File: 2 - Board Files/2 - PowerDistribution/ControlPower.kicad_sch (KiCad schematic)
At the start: 0 parts

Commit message: Part values for power input stage
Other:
- note added: "Switching Regulator A, 16V->3.3V Switching Regulator B, 5V->3.3V IF USB 5V PRESENT: DISABLE SWITCHER A, ENABLE SWITCHER B OTHERWISE, ENABLE SWITCHER A, DISABLE SWITCHER B Ensure hold up adequate to regulate during the switch!!"
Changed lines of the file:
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@@
 (kicad_sch (version 20211123) (generator eeschema)
   (paper "A4")
+  (text "Switching Regulator A, 16V->3.3V\nSwitching Regulator B, 5V->3.3V\n\nIF USB 5V PRESENT:\n\nDISABLE SWITCHER A, ENABLE SWITCHER B\n\nOTHERWISE,\n\nENABLE SWITCHER A, DISABLE SWITCHER B\n\nEnsure hold up adequate to regulate during the switch!!"
+    (at 17.78 39.37 0)
+    (effects (font (size 1.27 1.27)) (justify left bottom))
+  )
 )

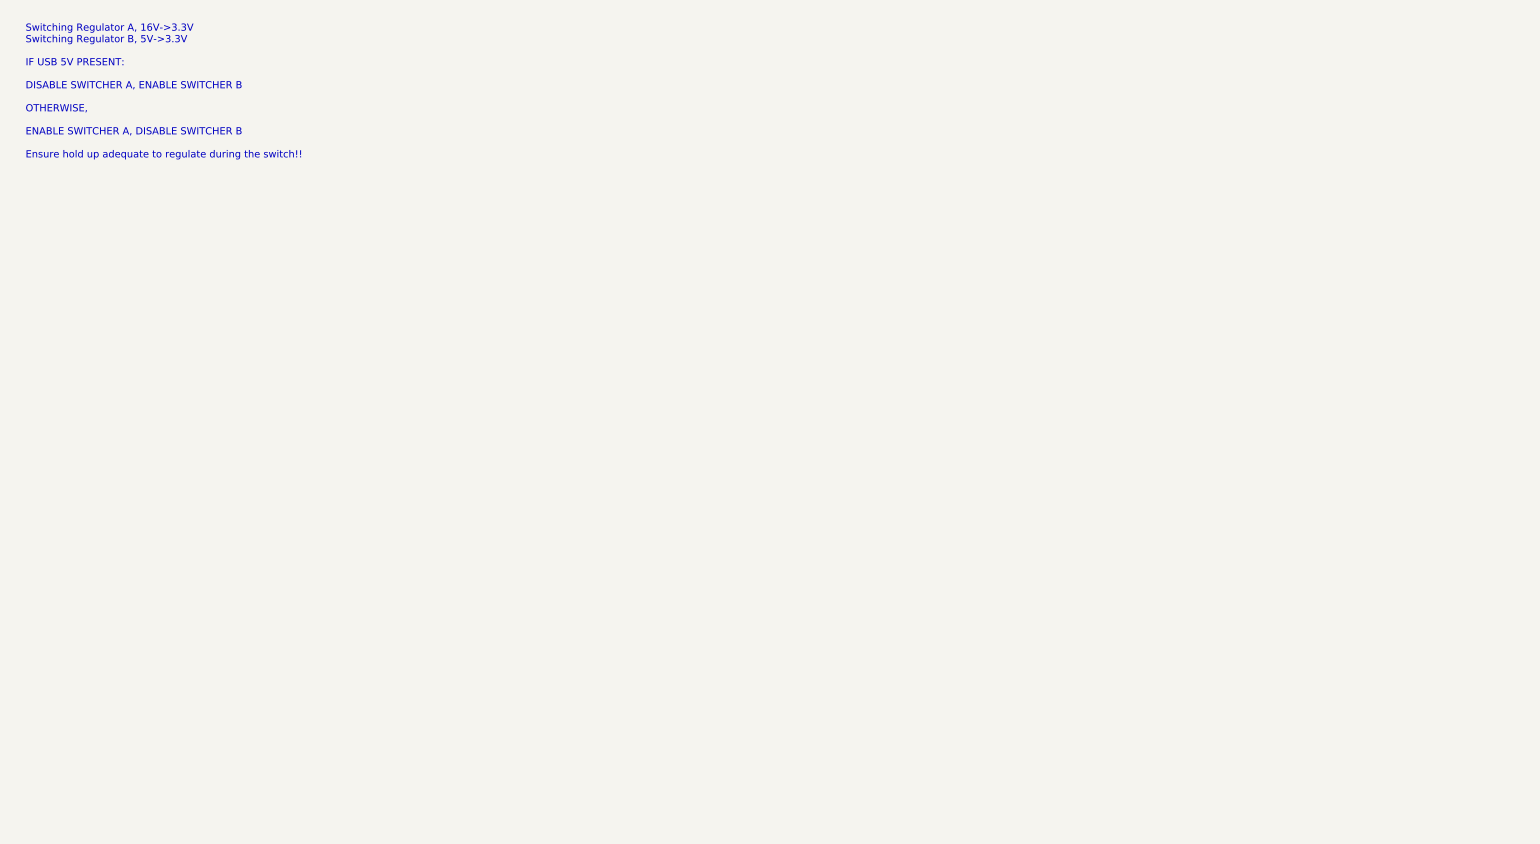
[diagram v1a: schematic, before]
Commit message: Added switching regulator
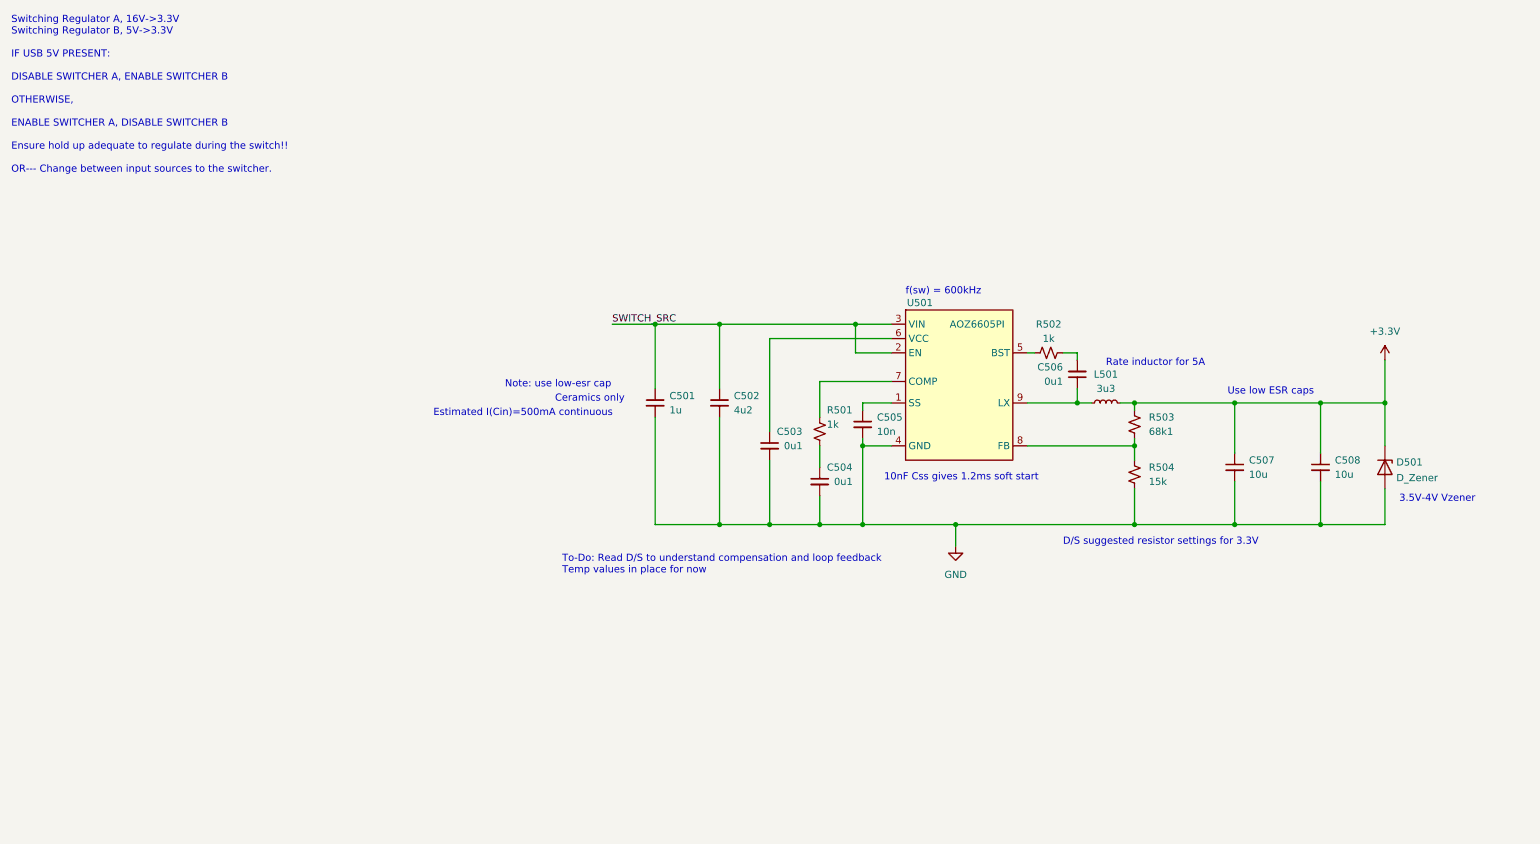
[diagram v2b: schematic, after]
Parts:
- added C501: 1u, Capacitor_SMD:C_0805_2012Metric, symbol Device:C_Small
- added C502: 4u2, Capacitor_SMD:C_0805_2012Metric, symbol Device:C_Small
- added C503, C504, C506: 0u1, Capacitor_SMD:C_0402_1005Metric, symbol Device:C_Small
- added C505: 10n, Capacitor_SMD:C_0402_1005Metric, symbol Device:C_Small
- added C507, C508: 10u, Capacitor_SMD:CP_Elec_6.3x5.4, symbol Device:C_Small
- added D501: D_Zener, Diode_SMD:D_SOD-323, symbol Device:D_Zener
- added L501: 3u3, Inductor_SMD:L_12x12mm_H4.5mm, symbol Device:L_Small
- added R501, R502: 1k, Resistor_SMD:R_0402_1005Metric, symbol Device:R_Small_US
- added R503: 68k1, Resistor_SMD:R_0402_1005Metric, symbol Device:R_Small_US
- added R504: 15k, Resistor_SMD:R_0402_1005Metric, symbol Device:R_Small_US
- added U501: AOZ6605PI, Package_SO:SOIC-8-1EP_3.9x4.9mm_P1.27mm_EP2.95x4.9mm_Mask2.71x3.4mm, symbol QuadrotorLib:AOZ6605PI
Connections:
- new net: R501.1, U501.7 (COMP)
- new net: C504.1, R501.2
- new net: C506.1, L501.1, U501.9 (LX)
- new net: C506.2, R502.1
- new net: R502.2, U501.5 (BST)
- new net: C503.1, U501.6 (VCC)
- new net: C505.1, U501.1 (SS)
- new net: R503.2, R504.1, U501.8 (FB)
- new net +3.3V: C507.1, C508.1, D501.1 (K), L501.2, R503.1
- new net GND: C501.2, C502.2, C503.2, C504.2, C505.2, C507.2, C508.2, D501.2 (A), R504.2, U501.4 (GND)
- new net SWITCH_SRC: C501.1, C502.1, U501.2 (EN), U501.3 (VIN)
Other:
- note added: "10nF Css gives 1.2ms soft start"
- note added: "3.5V-4V Vzener"
- note added: "Ceramics only"
- note added: "D/S suggested resistor settings for 3.3V"
- note added: "Estimated I(Cin)=500mA continuous"
- note added: "Note: use low-esr cap"
- note added: "Rate inductor for 5A"
- note added: "Switching Regulator A, 16V->3.3V Switching Regulator B, 5V->3.3V IF USB 5V PRESENT: DISABLE SWITCHER A, ENABLE SWITCHER B OTHERWISE, ENABLE SWITCHER A, DISABLE SWITCHER B Ensure hold up adequate to regulate during the switch!! OR--- Change between input sources to the switcher."
- note added: "To-Do: Read D/S to understand compensation and loop feedback Temp values in place for now"
- note added: "Use low ESR caps"
- note added: "f(sw) = 600kHz"
- note removed: "Switching Regulator A, 16V->3.3V Switching Regulator B, 5V->3.3V IF USB 5V PRESENT: DISABLE SWITCHER A, ENABLE SWITCHER B OTHERWISE, ENABLE SWITCHER A, DISABLE SWITCHER B Ensure hold up adequate to regulate during the switch!!"

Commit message: Switching regulator changes
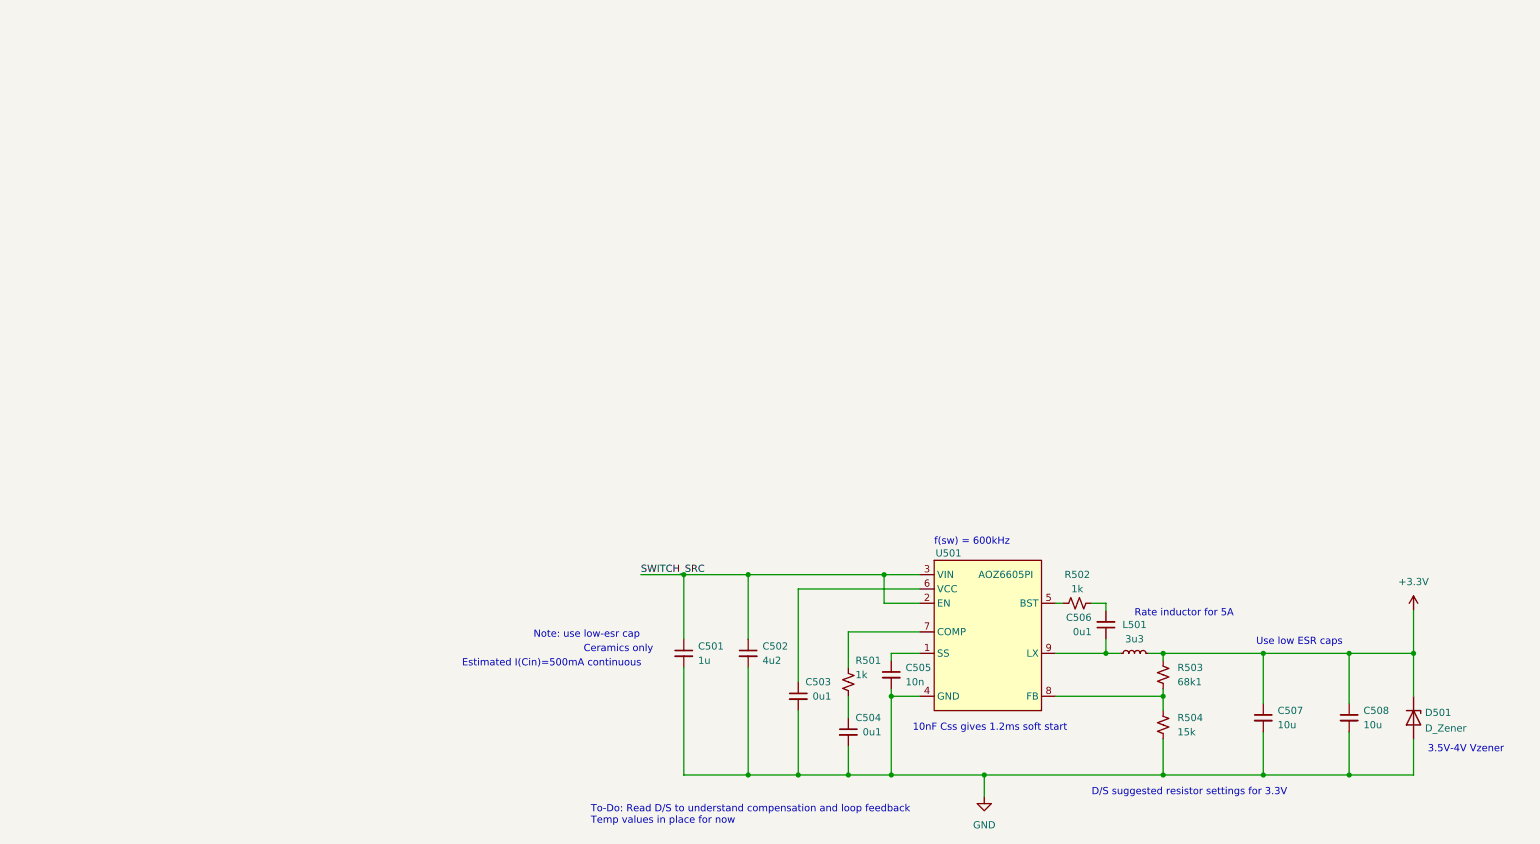
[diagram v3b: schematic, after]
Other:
- note removed: "Switching Regulator A, 16V->3.3V Switching Regulator B, 5V->3.3V IF USB 5V PRESENT: DISABLE SWITCHER A, ENABLE SWITCHER B OTHERWISE, ENABLE SWITCHER A, DISABLE SWITCHER B Ensure hold up adequate to regulate during the switch!! OR--- Change between input sources to the switcher."
- moved on the sheet: C501, C502, C503, C504, C505, C506, C507, C508, D501, L501, R501, R502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

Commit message: Motor drive initial work
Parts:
- added D502, D503: D, Diode_SMD:D_SMC, symbol Device:D
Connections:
- net SWITCH_SRC: now also D502.1 (K), D503.1 (K)
- new net VDC: D502.2 (A)
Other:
- note added: "Need to take in 8-16V DC input by default. Overridden by USB5V if unavailable or bad power"
- note added: "VDC = 8-16VDC input"
- moved on the sheet: C501, C502, C503, C504, C505, C506, C507, C508, D501, L501, R501, R502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
